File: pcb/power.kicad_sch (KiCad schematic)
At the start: 18 parts, among them J4 external supply, U4 RT9080-33GJ5, U5 TP4056

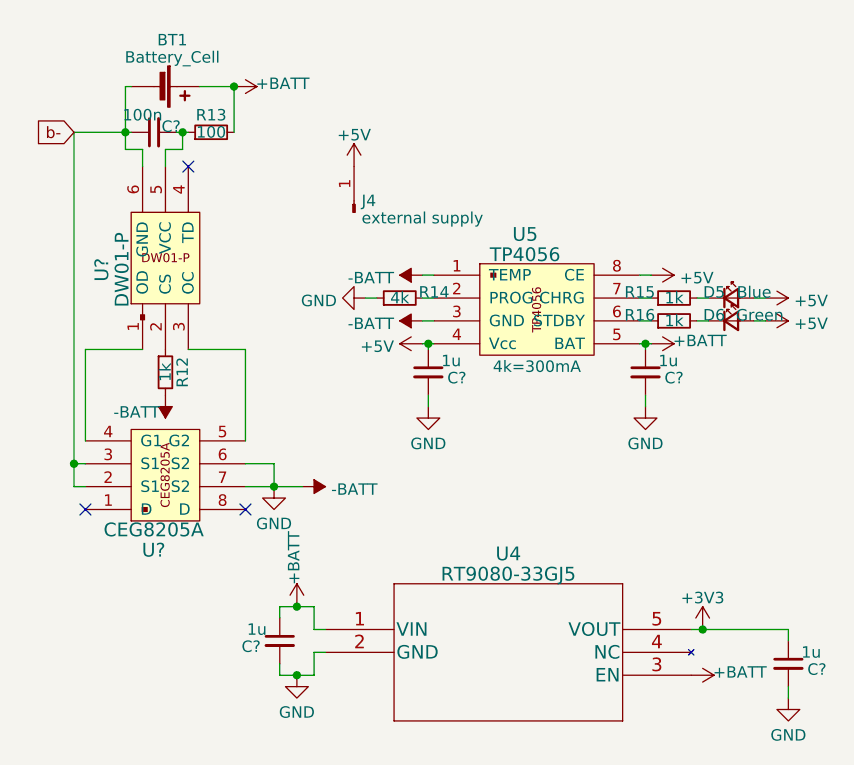
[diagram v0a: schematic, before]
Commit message: Fix low power issues
- Fix spurious EPD wakeups by adding pull-up to EPD reset line
- Reduce power consumption by switching sensors off with mosfet
- Connect button to reset to reduce power by not needing rtc gpio
- Add solder jumper for silent boot
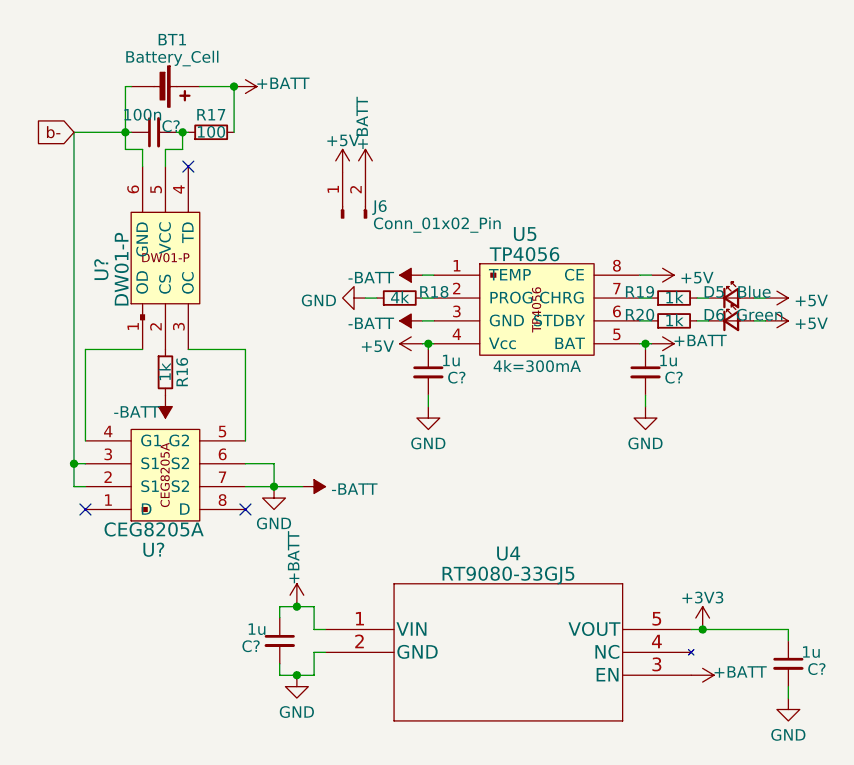
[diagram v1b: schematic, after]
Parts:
- removed J4: external supply, Connector_PinHeader_2.54mm:PinHeader_1x01_P2.54mm_Vertical, symbol Connector:Conn_01x01_Pin
- added J6: Conn_01x02_Pin, Connector_PinHeader_2.54mm:PinHeader_1x02_P2.54mm_Vertical, symbol Connector:Conn_01x02_Pin
- renumbered R12 to R16, R13 to R17, R14 to R18, R15 to R19, R16 to R20
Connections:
- net +5V: now also J6.1 (Pin_1)
- net +BATT: now also J6.2 (Pin_2)

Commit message: Replace b- net with -Battery
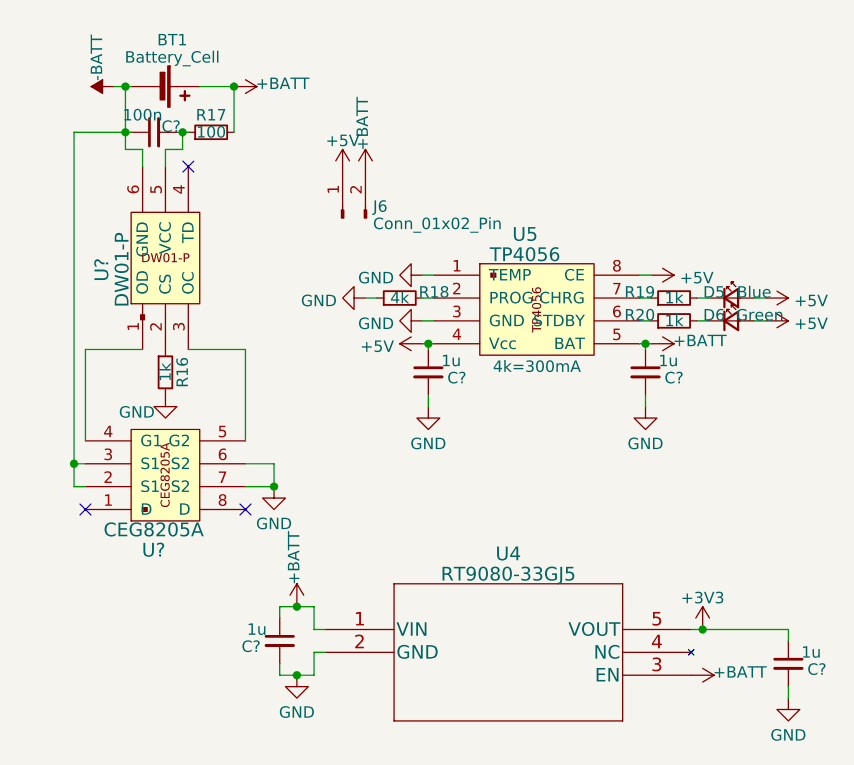
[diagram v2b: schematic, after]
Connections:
- net b- is gone; now on net -BATT: BT1.2 (-), C?.1, U?.2 (S1), U?.3 (S1), U?.6 (GND)
- net -BATT: no longer C?.2, C?.2, C?.2, C?.2, R16.2, R18.1, U4.2 (GND), U5.1 (TEMP), U5.3 (GND), U5.9 (HeatPad), U?.6 (S2), U?.7 (S2)
- new net GND: C?.2, C?.2, C?.2, C?.2, R16.2, R18.1, U4.2 (GND), U5.1 (TEMP), U5.3 (GND), U5.9 (HeatPad), U?.6 (S2), U?.7 (S2)
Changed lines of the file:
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@@
   (junction (at 113.03 56.515) (diameter 0) (color 0 0 0 0)
+  )
+  (junction (at 79.375 27.94) (diameter 0) (color 0 0 0 0)
   )
   (junction (at 91.44 27.94) (diameter 0) (color 0 0 0 0)
@@
     (stroke (width 0) (type default))
   )
-  (wire (pts (xy 95.885 72.39) (xy 99.06 72.39))
-    (stroke (width 0) (type default))
-  )
   (wire (pts (xy 142.24 88.265) (xy 143.51 88.265))
     (stroke (width 0) (type default))
@@
     (stroke (width 0) (type default))
   )
+  (wire (pts (xy 78.105 27.94) (xy 79.375 27.94))
+    (stroke (width 0) (type default))
+  )
   (wire (pts (xy 136.525 51.435) (xy 137.795 51.435))
     (stroke (width 0) (type default))
@@
     (stroke (width 0) (type default))
   )
-  (global_label "b-" (shape input) (at 73.66 33.02 180) (fields_autoplaced)
-    (effects (font (size 1.27 1.27)) (justify right))
-    (property "Intersheetrefs" "${INTERSHEET_REFS}" (at 68.0328 33.02 0)
-      (effects (font (size 1.27 1.27)) (justify right) hide)
-    )
-  )
   (symbol (lib_id "power:GND") (at 95.885 72.39 0) (mirror y) (unit 1)
     (in_bom yes) (on_board yes) (dnp no) (fields_autoplaced)
@@
     )
   )
-  (symbol (lib_id "power:-BATT") (at 99.06 72.39 270) (mirror x) (unit 1)
-    (in_bom yes) (on_board yes) (dnp no) (fields_autoplaced)
-    (property "Reference" "#PWR032" (at 95.25 72.39 0)
-      (effects (font (size 1.27 1.27)) hide)
-    )
-    (property "Value" "-BATT" (at 102.235 72.7068 90)
-      (effects (font (size 1.27 1.27)) (justify left))
-    )
-    (property "Footprint" "" (at 99.06 72.39 0)
-      (effects (font (size 1.27 1.27)) hide)
-    )
-    (property "Datasheet" "" (at 99.06 72.39 0)
-      (effects (font (size 1.27 1.27)) hide)
-    )
-    (pin "1")
-    (instances
-      (project "RoomSensor"
+  (symbol (lib_id "power:GND") (at 83.82 62.23 0) (mirror y) (unit 1)
+    (in_bom yes) (on_board yes) (dnp no)
+    (property "Reference" "#PWR?" (at 83.82 68.58 0)
+      (effects (font (size 1.27 1.27)) hide)
+    )
+    (property "Value" "GND" (at 80.645 64.135 0)
+      (effects (font (size 1.27 1.27)))
+    )
+    (property "Footprint" "" (at 83.82 62.23 0)
+      (effects (font (size 1.27 1.27)) hide)
+    )
+    (property "Datasheet" "" (at 83.82 62.23 0)
+      (effects (font (size 1.27 1.27)) hide)
+    )
+    (pin "1")
+    (instances
+      (project "RoomSensor"
+        (path "/df5fb727-aab3-46b2-bf4f-cd58d6f76ee2"
+          (reference "#PWR?") (unit 1)
+        )
         (path "/df5fb727-aab3-46b2-bf4f-cd58d6f76ee2/d94c8d32-e4e6-42df-bd50-6135d824efff"
           (reference "#PWR032") (unit 1)
@@
         (path "/df5fb727-aab3-46b2-bf4f-cd58d6f76ee2/d94c8d32-e4e6-42df-bd50-6135d824efff"
           (reference "D5") (unit 1)
-        )
-      )
-    )
-  )
-  (symbol (lib_id "power:-BATT") (at 112.395 48.895 90) (mirror x) (unit 1)
-    (in_bom yes) (on_board yes) (dnp no) (fields_autoplaced)
-    (property "Reference" "#PWR036" (at 116.205 48.895 0)
-      (effects (font (size 1.27 1.27)) hide)
-    )
-    (property "Value" "-BATT" (at 109.22 49.2118 90)
-      (effects (font (size 1.27 1.27)) (justify left))
-    )
-    (property "Footprint" "" (at 112.395 48.895 0)
-      (effects (font (size 1.27 1.27)) hide)
-    )
-    (property "Datasheet" "" (at 112.395 48.895 0)
-      (effects (font (size 1.27 1.27)) hide)
-    )
-    (pin "1")
-    (instances
-      (project "RoomSensor"
-        (path "/df5fb727-aab3-46b2-bf4f-cd58d6f76ee2/d94c8d32-e4e6-42df-bd50-6135d824efff"
-          (reference "#PWR036") (unit 1)
         )
       )
@@
     )
   )
+  (symbol (lib_id "power:GND") (at 112.395 53.975 270) (mirror x) (unit 1)
+    (in_bom yes) (on_board yes) (dnp no) (fields_autoplaced)
+    (property "Reference" "#PWR?" (at 106.045 53.975 0)
+      (effects (font (size 1.27 1.27)) hide)
+    )
+    (property "Value" "GND" (at 109.2201 54.2918 90)
+      (effects (font (size 1.27 1.27)) (justify right))
+    )
+    (property "Footprint" "" (at 112.395 53.975 0)
+      (effects (font (size 1.27 1.27)) hide)
+    )
+    (property "Datasheet" "" (at 112.395 53.975 0)
+      (effects (font (size 1.27 1.27)) hide)
+    )
+    (pin "1")
+    (instances
+      (project "RoomSensor"
+        (path "/df5fb727-aab3-46b2-bf4f-cd58d6f76ee2"
+          (reference "#PWR?") (unit 1)
+        )
+        (path "/df5fb727-aab3-46b2-bf4f-cd58d6f76ee2/d94c8d32-e4e6-42df-bd50-6135d824efff"
+          (reference "#PWR036") (unit 1)
+        )
+      )
+    )
+  )
   (symbol (lib_id "power:+BATT") (at 91.44 27.94 270) (unit 1)
     (in_bom yes) (on_board yes) (dnp no)
@@
     )
   )
-  (symbol (lib_id "power:-BATT") (at 83.82 62.23 180) (unit 1)
-    (in_bom yes) (on_board yes) (dnp no)
-    (property "Reference" "#PWR027" (at 83.82 58.42 0)
-      (effects (font (size 1.27 1.27)) hide)
-    )
-    (property "Value" "-BATT" (at 83.185 64.135 0)
+  (symbol (lib_id "power:-BATT") (at 78.105 27.94 90) (unit 1)
+    (in_bom yes) (on_board yes) (dnp no)
+    (property "Reference" "#PWR027" (at 81.915 27.94 0)
+      (effects (font (size 1.27 1.27)) hide)
+    )
+    (property "Value" "-BATT" (at 76.2 27.305 0)
       (effects (font (size 1.27 1.27)) (justify left))
     )
-    (property "Footprint" "" (at 83.82 62.23 0)
-      (effects (font (size 1.27 1.27)) hide)
-    )
-    (property "Datasheet" "" (at 83.82 62.23 0)
+    (property "Footprint" "" (at 78.105 27.94 0)
+      (effects (font (size 1.27 1.27)) hide)
+    )
+    (property "Datasheet" "" (at 78.105 27.94 0)
       (effects (font (size 1.27 1.27)) hide)
     )
@@
     )
   )
-  (symbol (lib_id "power:-BATT") (at 112.395 53.975 90) (mirror x) (unit 1)
-    (in_bom yes) (on_board yes) (dnp no) (fields_autoplaced)
-    (property "Reference" "#PWR037" (at 116.205 53.975 0)
-      (effects (font (size 1.27 1.27)) hide)
-    )
-    (property "Value" "-BATT" (at 109.22 54.2918 90)
-      (effects (font (size 1.27 1.27)) (justify left))
-    )
-    (property "Footprint" "" (at 112.395 53.975 0)
-      (effects (font (size 1.27 1.27)) hide)
-    )
-    (property "Datasheet" "" (at 112.395 53.975 0)
-      (effects (font (size 1.27 1.27)) hide)
-    )
-    (pin "1")
-    (instances
-      (project "RoomSensor"
+  (symbol (lib_id "Device:R_Small") (at 88.9 33.02 90) (unit 1)
+    (in_bom yes) (on_board yes) (dnp no)
+    (property "Reference" "R17" (at 88.9 31.115 90)
+      (effects (font (size 1.27 1.27)))
+    )
+    (property "Value" "100" (at 88.9 33.02 90)
+      (effects (font (size 1.27 1.27)))
+    )
+    (property "Footprint" "Resistor_SMD:R_0603_1608Metric" (at 88.9 33.02 0)
+      (effects (font (size 1.27 1.27)) hide)
+    )
+    (property "Datasheet" "~" (at 88.9 33.02 0)
+      (effects (font (size 1.27 1.27)) hide)
+    )
+    (pin "1")
+    (pin "2")
+    (instances
+      (project "RoomSensor"
+        (path "/df5fb727-aab3-46b2-bf4f-cd58d6f76ee2/d94c8d32-e4e6-42df-bd50-6135d824efff"
+          (reference "R17") (unit 1)
+        )
+      )
+    )
+  )
+  (symbol (lib_id "power:GND") (at 112.395 48.895 270) (mirror x) (unit 1)
+    (in_bom yes) (on_board yes) (dnp no) (fields_autoplaced)
+    (property "Reference" "#PWR?" (at 106.045 48.895 0)
+      (effects (font (size 1.27 1.27)) hide)
+    )
+    (property "Value" "GND" (at 109.2201 49.2118 90)
+      (effects (font (size 1.27 1.27)) (justify right))
+    )
+    (property "Footprint" "" (at 112.395 48.895 0)
+      (effects (font (size 1.27 1.27)) hide)
+    )
+    (property "Datasheet" "" (at 112.395 48.895 0)
+      (effects (font (size 1.27 1.27)) hide)
+    )
+    (pin "1")
+    (instances
+      (project "RoomSensor"
+        (path "/df5fb727-aab3-46b2-bf4f-cd58d6f76ee2"
+          (reference "#PWR?") (unit 1)
+        )
         (path "/df5fb727-aab3-46b2-bf4f-cd58d6f76ee2/d94c8d32-e4e6-42df-bd50-6135d824efff"
           (reference "#PWR037") (unit 1)
         )
       )
-    )
-  )
-  (symbol (lib_id "Device:R_Small") (at 88.9 33.02 90) (unit 1)
-    (in_bom yes) (on_board yes) (dnp no)
-    (property "Reference" "R17" (at 88.9 31.115 90)
-      (effects (font (size 1.27 1.27)))
-    )
-    (property "Value" "100" (at 88.9 33.02 90)
-      (effects (font (size 1.27 1.27)))
-    )
-    (property "Footprint" "Resistor_SMD:R_0603_1608Metric" (at 88.9 33.02 0)
-      (effects (font (size 1.27 1.27)) hide)
-    )
-    (property "Datasheet" "~" (at 88.9 33.02 0)
-      (effects (font (size 1.27 1.27)) hide)
-    )
-    (pin "1")
-    (pin "2")
-    (instances
-      (project "RoomSensor"
-        (path "/df5fb727-aab3-46b2-bf4f-cd58d6f76ee2/d94c8d32-e4e6-42df-bd50-6135d824efff"
-          (reference "R17") (unit 1)
-        )
-      )
